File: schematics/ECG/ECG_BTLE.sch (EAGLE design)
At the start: 6 parts, among them IC1 ADS1293, IC3 LP2985

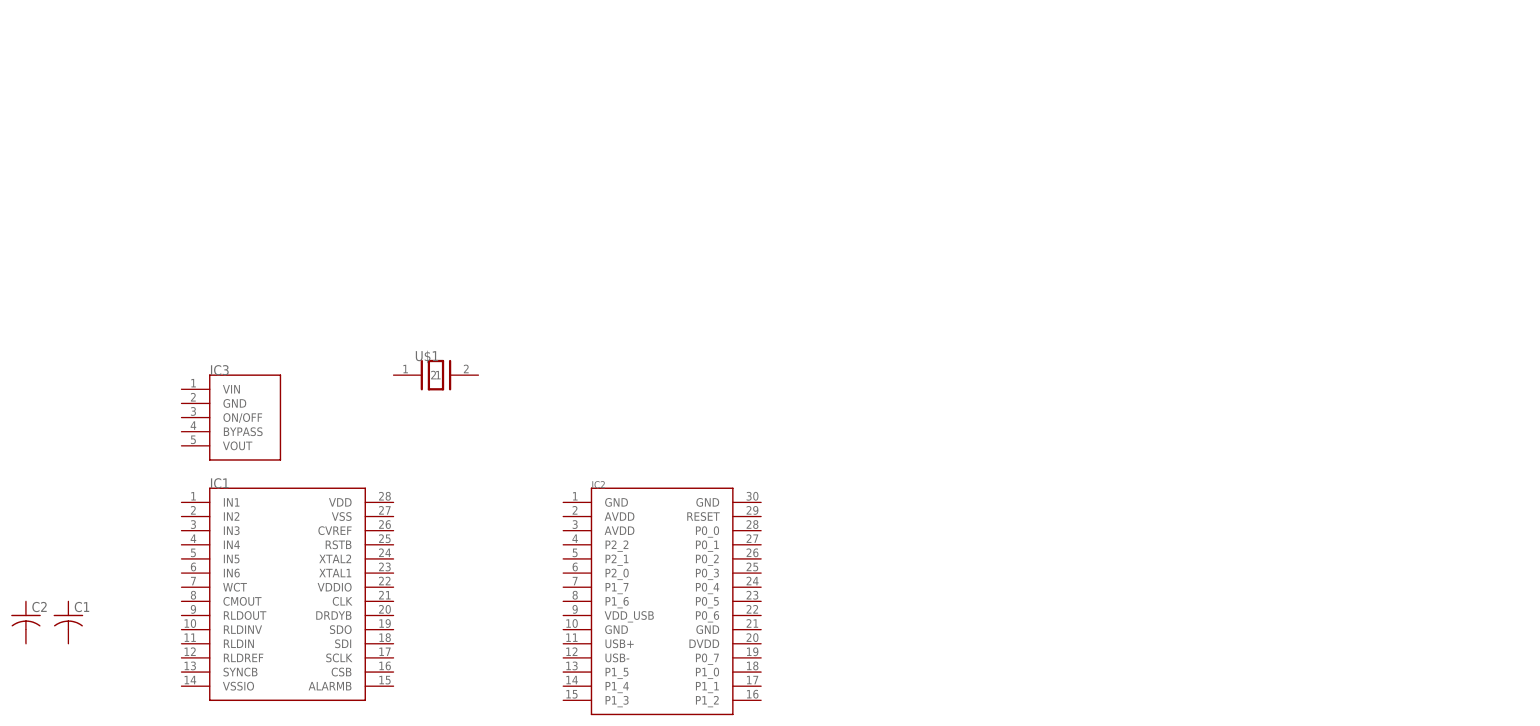
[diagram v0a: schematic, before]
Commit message: schematic update
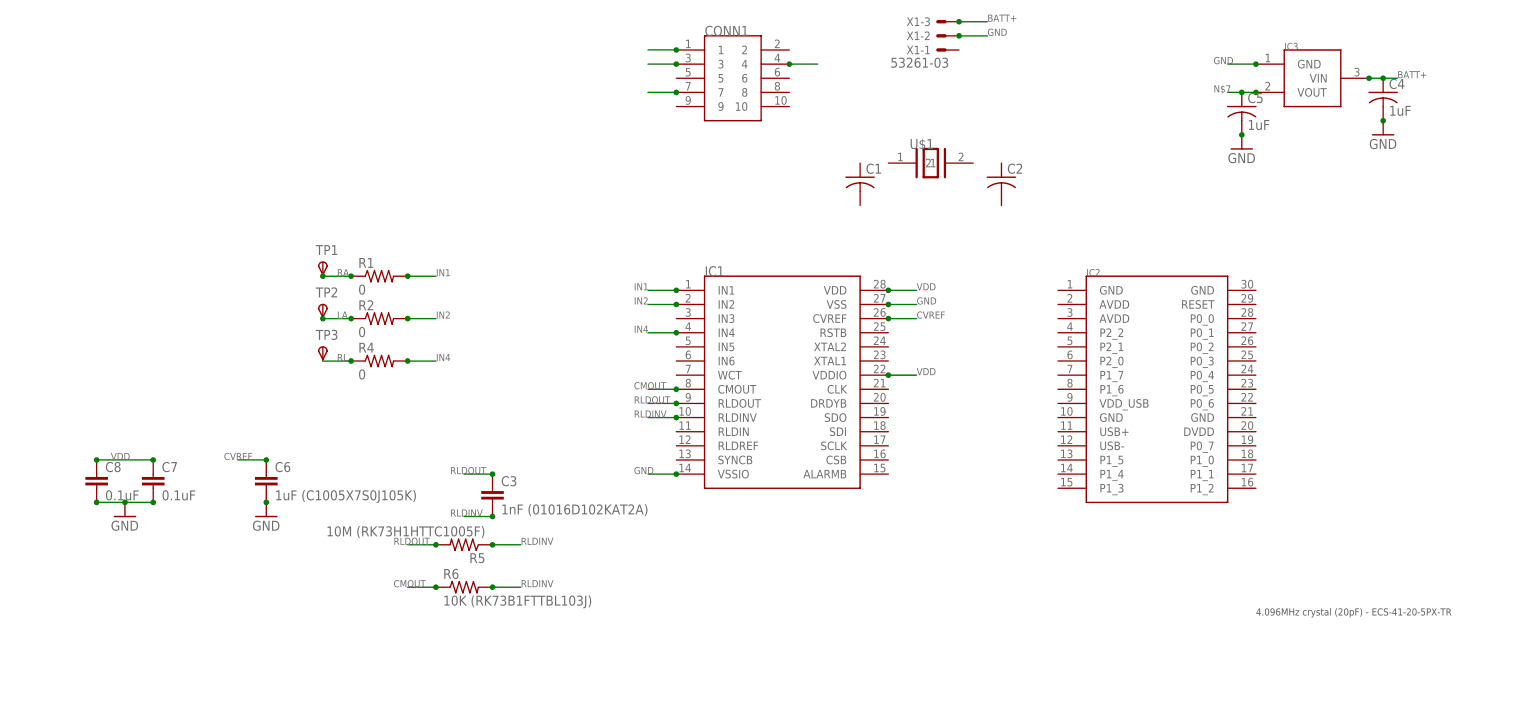
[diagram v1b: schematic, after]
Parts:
- added C3: 1nF (01016D102KAT2A), rcl:C-EUC0402
- added C4, C5: 1uF, rcl:C-USC0201
- added C6: 1uF (C1005X7S0J105K), rcl:C-EUC0402
- added C7, C8: 0.1uF, rcl:C-EUC0402
- added CONN1: 10POS_1.27MM_SMD, harwin:10POS_1.27MM_SMD
- added R1, R2, R4: 0, resistor:R-US_R0402
- added R5: 10M (RK73H1HTTC1005F), resistor:R-US_R0603
- added R6: 10K (RK73B1FTTBL103J), resistor:R-US_R0402
- added TP1, TP2, TP3: TPSTP08SQ, testpad:TPSTP08SQ
- added X1: 53261-03, con-molex:53261-03
- IC3: value LP2985 -> MCP1703; device ti:LP2985 -> microchip_regulators:MCP1703
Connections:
- new net BATT+: C4.1, IC3.VIN, X1-3.S
- new net CMOUT: IC1.CMOUT, R6.1
- new net CVREF: C6.1, IC1.CVREF
- new net GND: C4.2, C5.2, C6.2, C7.2, C8.2, IC1.VSS, IC1.VSSIO, IC3.GND, X1-2.S
- new net IN1: IC1.IN1, R1.2
- new net IN2: IC1.IN2, R2.2
- new net IN4: IC1.IN4, R4.2
- new net LA: R2.1, TP2.PP
- new net N$1: CONN1.4
- new net N$2: CONN1.3
- new net N$3: CONN1.7
- new net N$4: CONN1.1
- new net N$7: C5.1, IC3.VOUT
- new net RA: R1.1, TP1.PP
- new net RL: R4.1, TP3.PP
- new net RLDINV: C3.2, IC1.RLDINV, R5.1, R6.2
- new net RLDOUT: C3.1, IC1.RLDOUT, R5.2
- new net VDD: C7.1, C8.1, IC1.VDD, IC1.VDDIO
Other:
- note added: "4.096MHz crystal (20pF) - ECS-41-20-5PX-TR"
- moved on the sheet: C1, C2, IC1, IC2, U$1

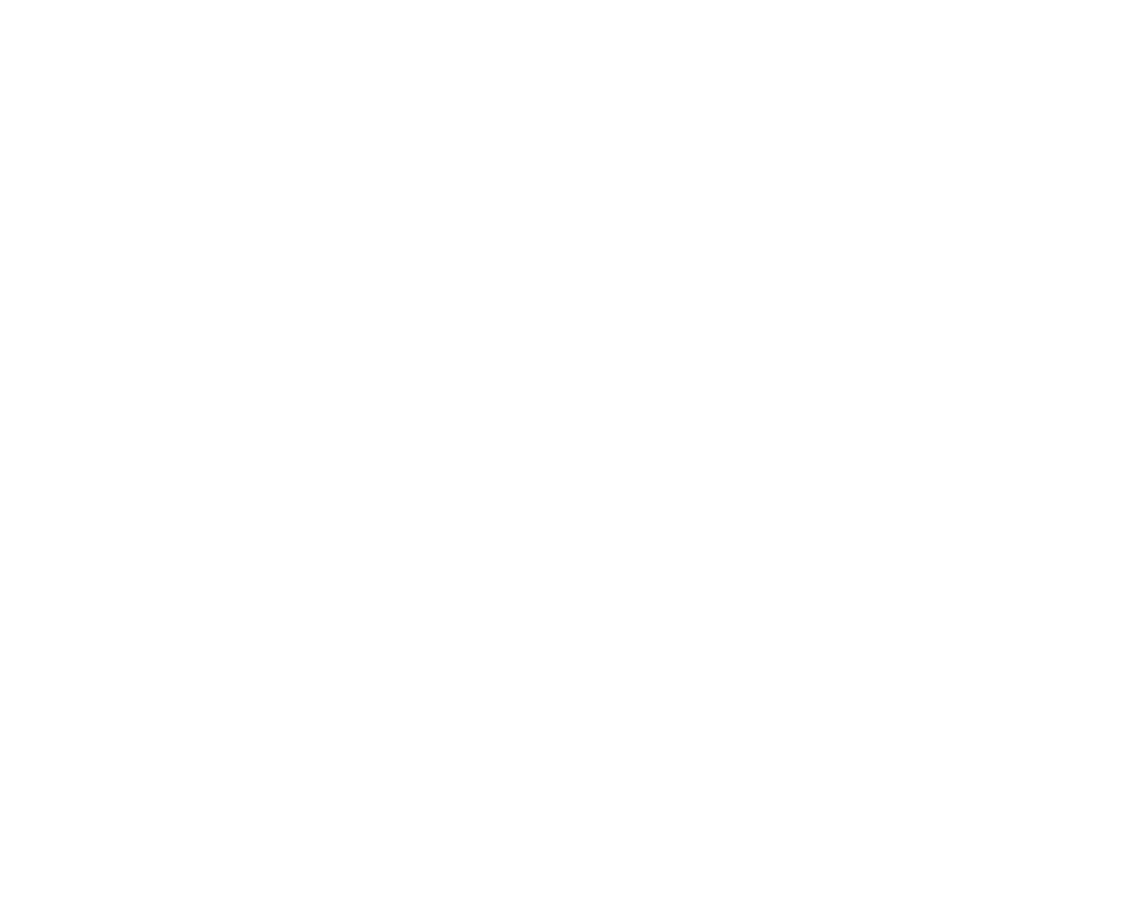
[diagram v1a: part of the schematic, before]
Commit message: adding individual BLE components instead of module for space saving purposes
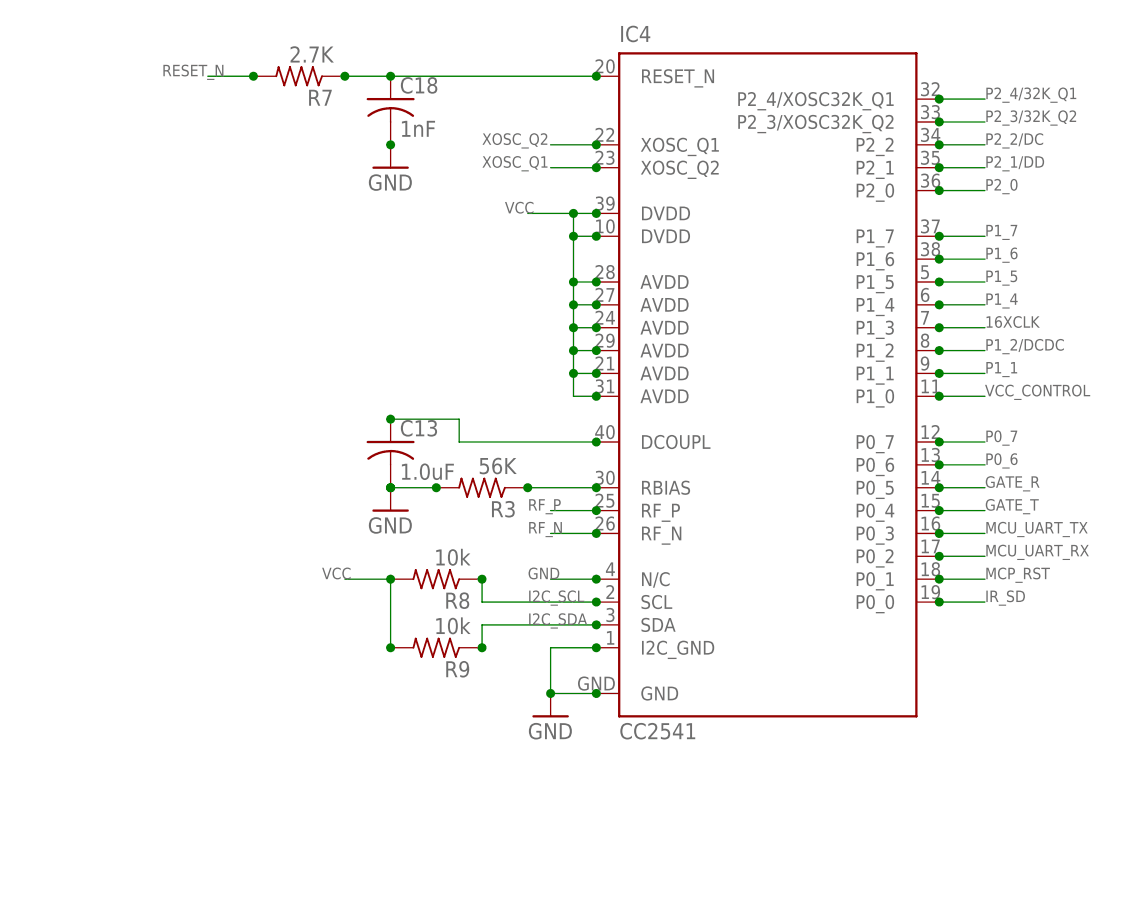
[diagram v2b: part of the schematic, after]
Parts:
- added C13: 1.0uF, rcl:C-USC0402
- added C18: 1nF, rcl:C-USC0402
- added IC4: CC2541, ST-CC254X:CC2541
- added R3: 56K, rcl:R-US_R0201
- added R7: 2.7K, rcl:R-US_R0201
- added R8, R9: 10k, rcl:R-US_R0201
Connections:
- new net 16XCLK: IC4.P1_3
- new net DCOUPL1: C13.1, IC4.DCOUPL
- new net GATE_R: IC4.P0_5
- new net GATE_T: IC4.P0_4
- new net I2C_SCL: IC4.SCL, R8.1
- new net I2C_SDA: IC4.SDA, R9.1
- new net IR_SD: IC4.P0_0
- new net MCP_RST: IC4.P0_1
- new net MCU_UART_RX: IC4.P0_2
- new net MCU_UART_TX: IC4.P0_3
- new net N$8: C18.1, IC4.RESET_N, R7.1
- new net P0_6: IC4.P0_6
- new net P0_7: IC4.P0_7
- new net P1_1: IC4.P1_1
- new net P1_2/DCDC: IC4.P1_2
- new net P1_4: IC4.P1_4
- new net P1_5: IC4.P1_5
- new net P1_6: IC4.P1_6
- new net P1_7: IC4.P1_7
- new net P2_0: IC4.P2_0
- new net P2_1/DD: IC4.P2_1
- new net P2_2/DC: IC4.P2_2
- new net P2_3/32K_Q2: IC4.P2_3/XOSC32K_Q2
- new net P2_4/32K_Q1: IC4.P2_4/XOSC32K_Q1
- new net RESET_N: R7.2
- new net RF_N: IC4.RF_N
- new net RF_P: IC4.RF_P
- new net R_BIAS: IC4.RBIAS, R3.1
- new net VCC: IC4.AVDD@1, IC4.AVDD@2, IC4.AVDD@3, IC4.AVDD@4, IC4.AVDD@5, IC4.AVDD@6, IC4.DVDD@1, IC4.DVDD@2, R8.2, R9.2
- new net VCC_CONTROL: IC4.P1_0
- new net XOSC_Q1: IC4.XOSC_Q2
- new net XOSC_Q2: IC4.XOSC_Q1
- net GND: now also C13.2, C18.2, IC4.GND, IC4.I2C_GND, IC4.N/C, R3.2

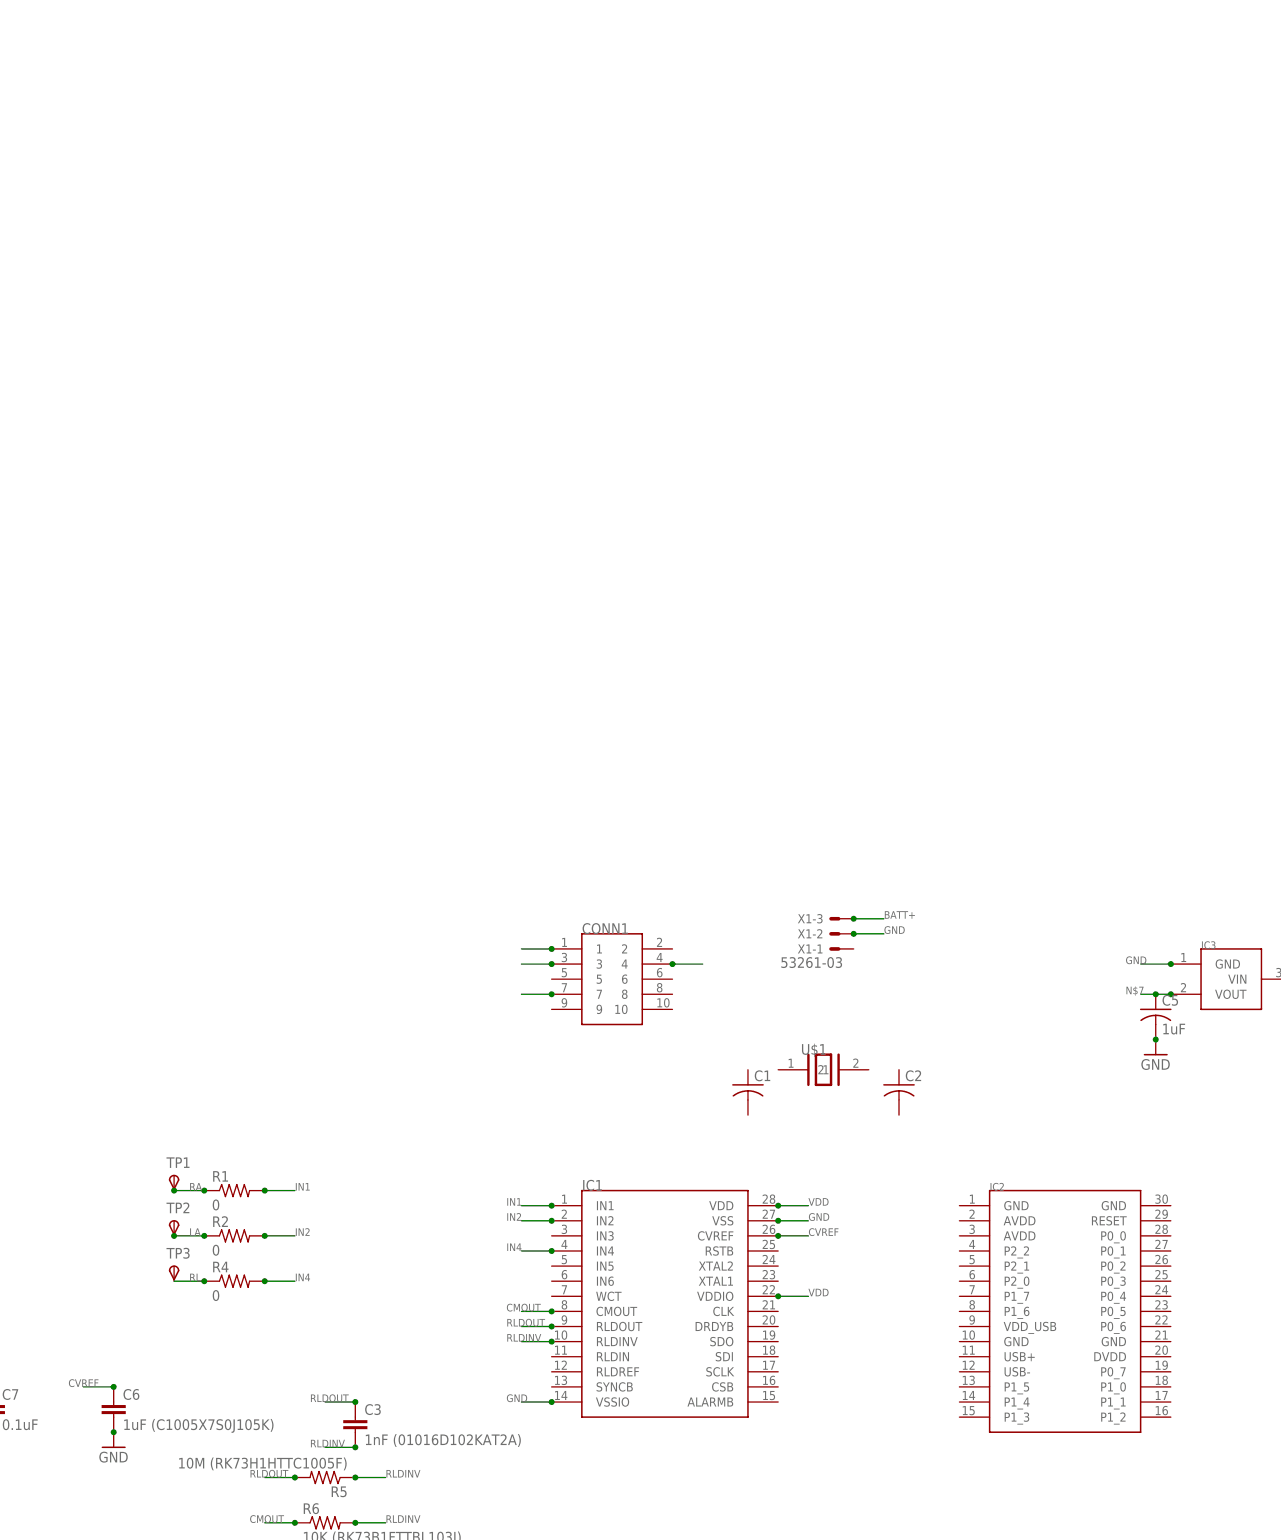
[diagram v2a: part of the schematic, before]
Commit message: added board to board connectors, removed BLE module
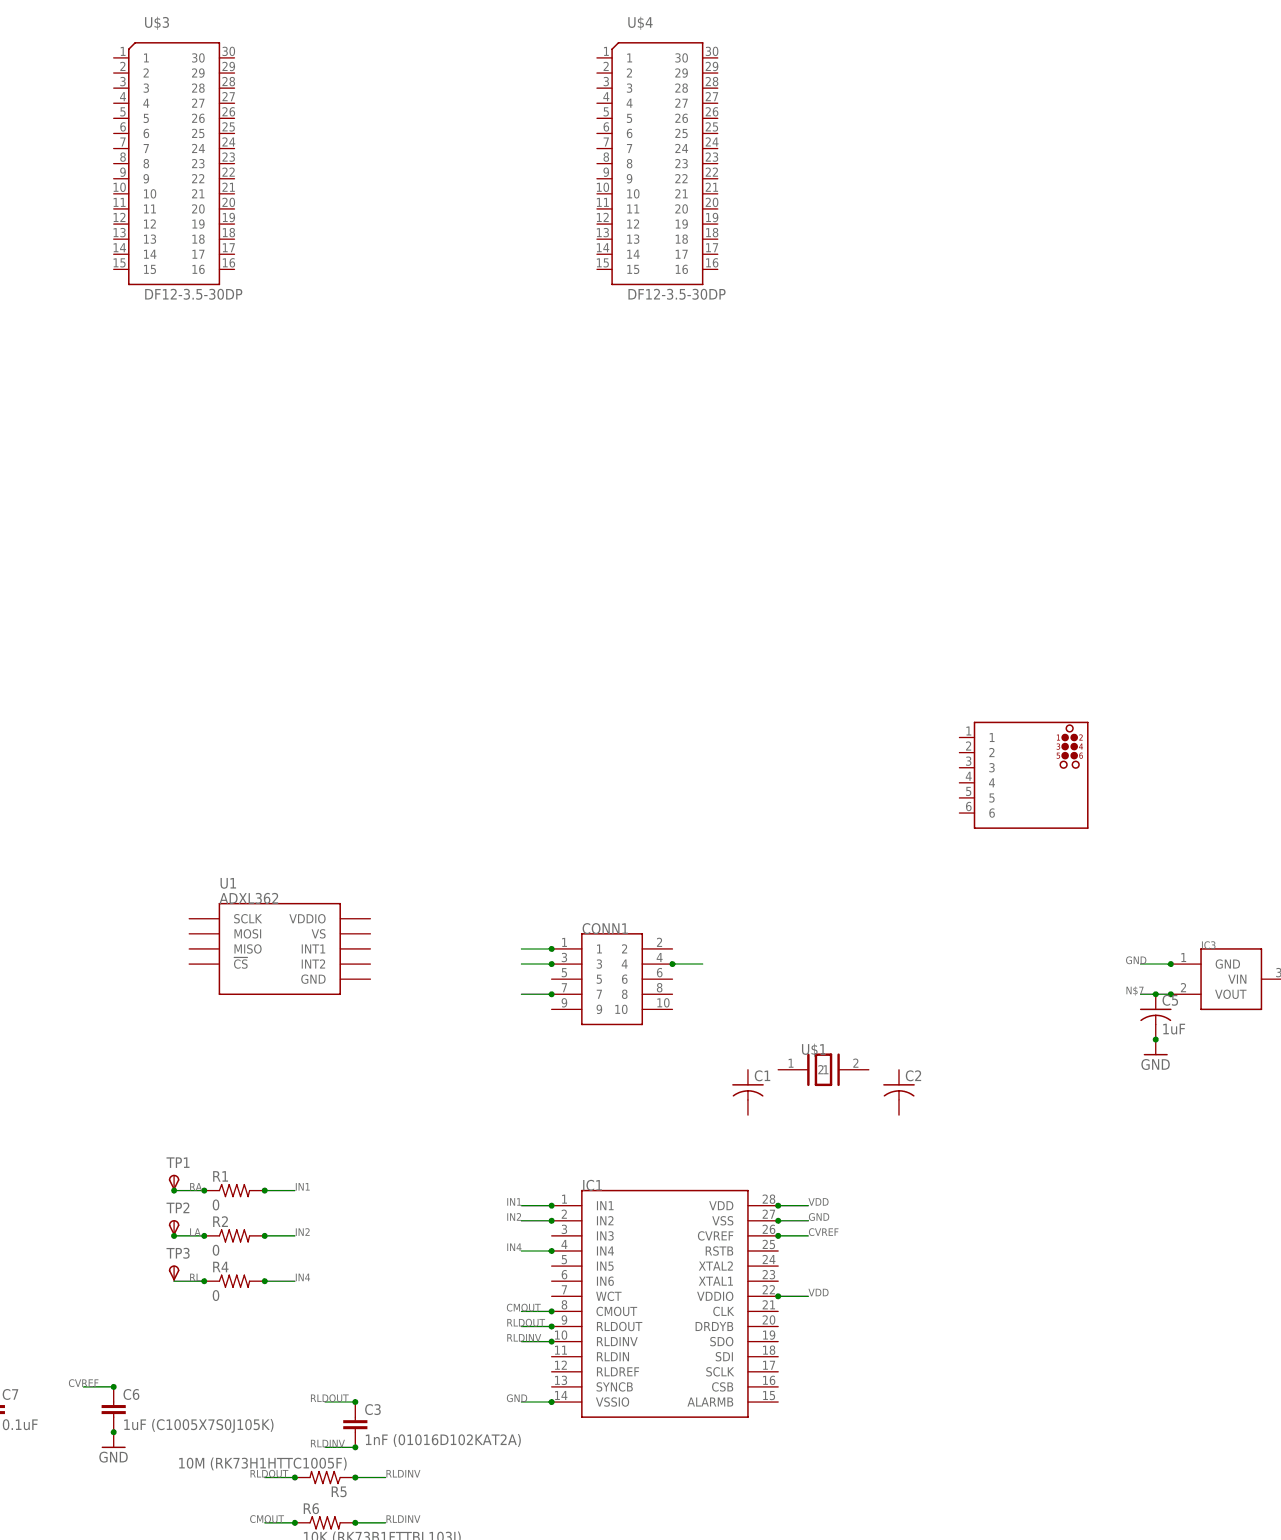
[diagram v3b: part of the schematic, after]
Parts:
- removed IC2: (no value), bluegiga:BLE112
- removed X1: 53261-03, con-molex:53261-03
- added U$2: TC2030-MCP-NL, tagconnect:TC2030-MCP-NL
- added U$3, U$4: DF12-3.5-30DP, hirose:DF12-3.5-30DP
- added U1: ADXL362, SparkFun-Sensors:ADXL362
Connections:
- net BATT+: no longer X1-3.S
- net GND: no longer X1-2.S
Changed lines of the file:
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@@
 <parts>
 <part name="IC1" library="texas_instruments" deviceset="ADS1293" device=""/>
-<part name="IC2" library="bluegiga" deviceset="BLE112" device=""/>
 <part name="C2" library="rcl" deviceset="C-US" device="C0201"/>
 <part name="U$1" library="ecs" deviceset="XTAL-CSM7" device=""/>
 <part name="CONN1" library="harwin" deviceset="10POS_1.27MM_SMD" device=""/>
 <part name="C1" library="rcl" deviceset="C-US" device="C0201"/>
-<part name="X1" library="con-molex" deviceset="53?-03" device="261"/>
 <part name="IC3" library="microchip_regulators" deviceset="MCP1703" device=""/>
 <part name="C4" library="rcl" deviceset="C-US" device="C0201" value="1uF"/>
@@
 <part name="R8" library="rcl" deviceset="R-US_" device="R0201" value="10k"/>
 <part name="R9" library="rcl" deviceset="R-US_" device="R0201" value="10k"/>
+<part name="U1" library="SparkFun-Sensors" deviceset="ADXL362" device="" value="ADXL362"/>
+<part name="U$2" library="tagconnect" deviceset="TC2030" device="-MCP-NL"/>
+<part name="U$3" library="hirose" deviceset="DF12-3.5-30DP" device=""/>
+<part name="U$4" library="hirose" deviceset="DF12-3.5-30DP" device=""/>
 </parts>
 <sheets>
@@
 <instances>
 <instance part="IC1" gate="IC" x="134.62" y="86.36"/>
-<instance part="IC2" gate="IC" x="203.2" y="88.9"/>
 <instance part="C2" gate="G$1" x="175.26" y="121.92"/>
 <instance part="U$1" gate="XTAL" x="162.56" y="124.46"/>
 <instance part="CONN1" gate="CONN" x="127" y="139.7"/>
 <instance part="C1" gate="G$1" x="149.86" y="121.92"/>
-<instance part="X1" gate="-1" x="165.1" y="144.78" rot="R180"/>
-<instance part="X1" gate="-2" x="165.1" y="147.32" rot="R180"/>
-<instance part="X1" gate="-3" x="165.1" y="149.86" rot="R180"/>
 <instance part="IC3" gate="IC" x="231.14" y="139.7"/>
 <instance part="C4" gate="G$1" x="243.84" y="137.16"/>
@@
 <instance part="R8" gate="G$1" x="396.24" y="99.06" rot="R180"/>
 <instance part="R9" gate="G$1" x="396.24" y="91.44" rot="R180"/>
+<instance part="U1" gate="G$1" x="71.12" y="144.78"/>
+<instance part="U$2" gate="G$1" x="198.12" y="172.72"/>
+<instance part="U$3" gate="CONN" x="53.34" y="274.32"/>
+<instance part="U$4" gate="CONN" x="134.62" y="274.32"/>
 </instances>
 <busses>
@@
 </net>
 <net name="GND" class="0">
-<segment>
-<pinref part="X1" gate="-2" pin="S"/>
-<wire x1="167.64" y1="147.32" x2="172.72" y2="147.32" width="0.1524" layer="91"/>
-<junction x="167.64" y="147.32"/>
-<label x="172.72" y="147.32" size="1.27" layer="95"/>
-</segment>
 <segment>
 <pinref part="IC3" gate="IC" pin="GND"/>
@@
 <net name="BATT+" class="0">
 <segment>
-<pinref part="X1" gate="-3" pin="S"/>
-<wire x1="167.64" y1="149.86" x2="172.72" y2="149.86" width="0.1524" layer="91"/>
-<junction x="167.64" y="149.86"/>
-<label x="172.72" y="149.86" size="1.27" layer="95"/>
-</segment>
-<segment>
 <pinref part="IC3" gate="IC" pin="VIN"/>
